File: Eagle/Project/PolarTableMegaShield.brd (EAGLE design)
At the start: 53.2 x 90.2 mm, 41 parts, among them IC2 LM358D, J10 LED + Radio, J3 Pi Connection, J5 IR Sensors, J6 Switch A + B, J7 Switch C + D, J8 Switch E + F, Q1 BC337, Q2 2N3906, Q3 2N3904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

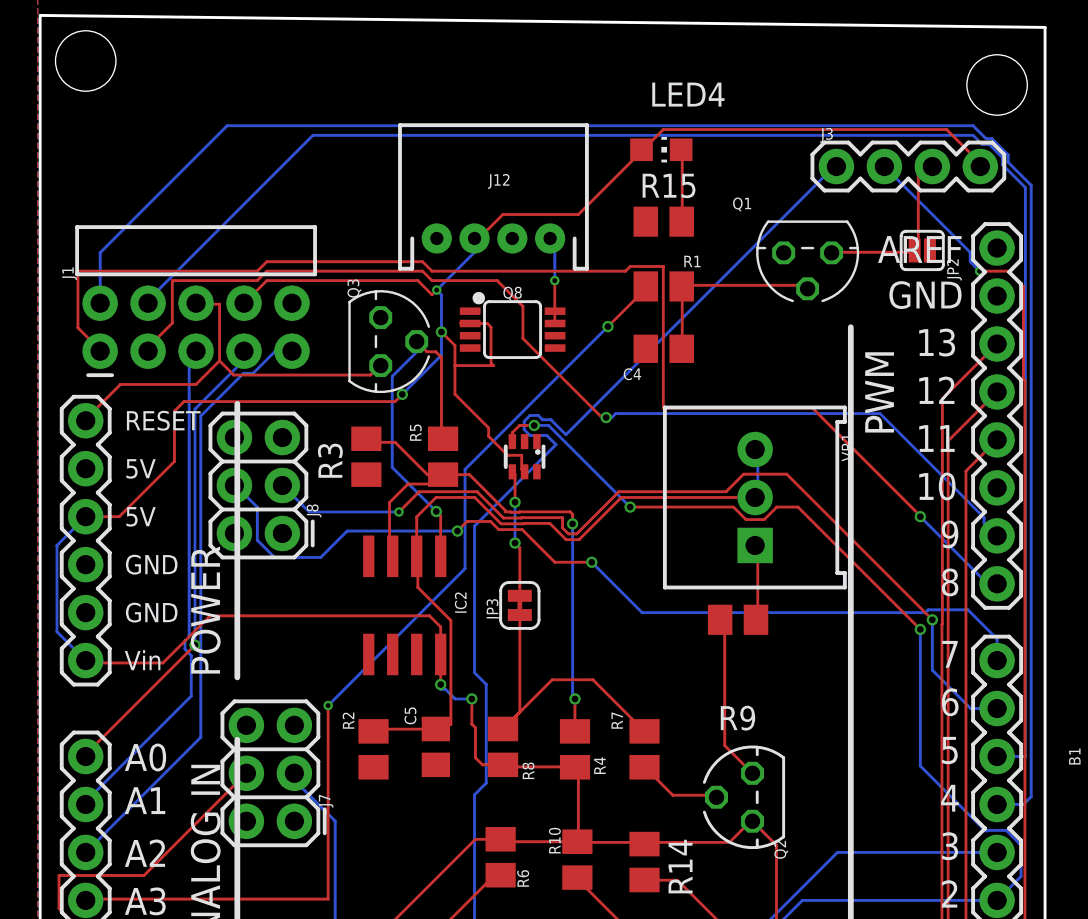
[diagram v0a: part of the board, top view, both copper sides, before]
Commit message: Changed the connector to be 6x2 so the shift reg could run at 3.3V
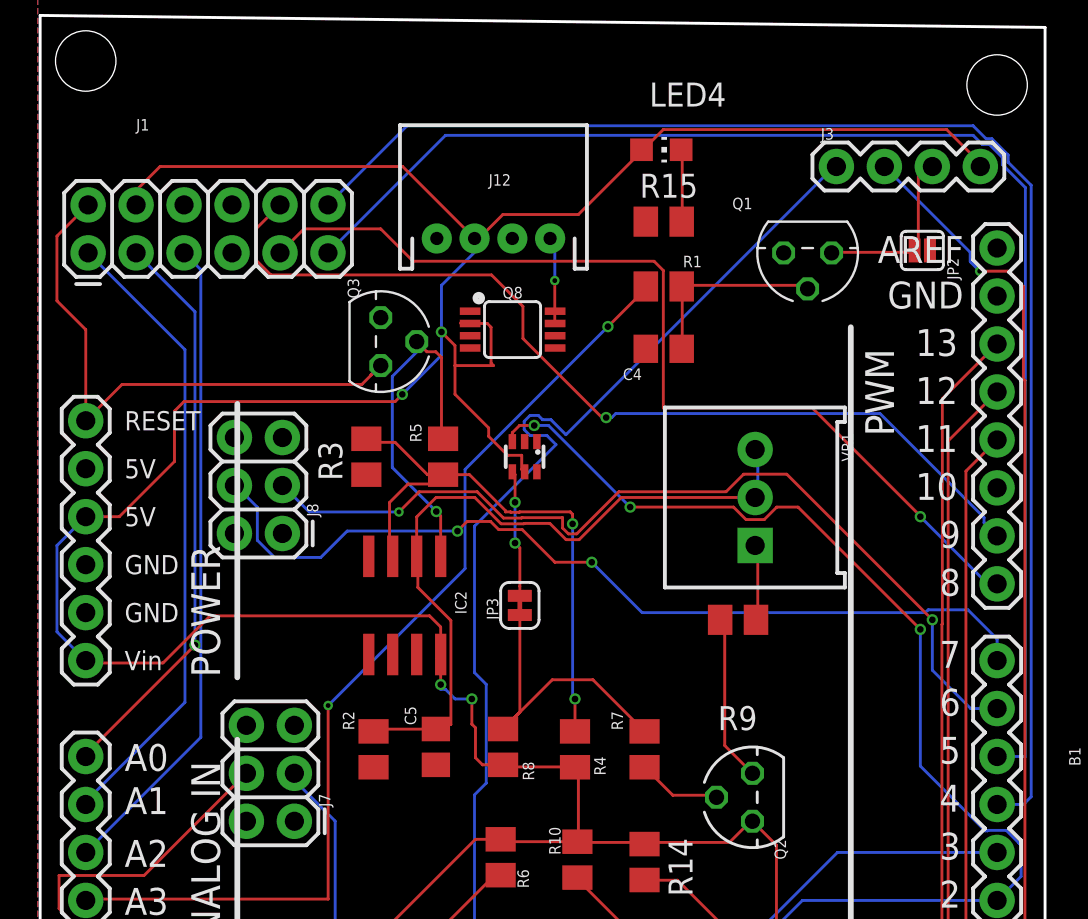
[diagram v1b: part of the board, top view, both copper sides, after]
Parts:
- J1: device SparkFun-Connectors:2X5-RA -> keir_library:2X6
- moved J1 6.94 mm to (2.54, 77.5), turned to 0 degrees
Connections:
- net !RES: now also J1.2; no longer J1.6
- net CLOCK: now also J1.1; no longer J1.5
- net DATA: now also J1.3; no longer J1.7
- net GND: now also J1.6, J1.8; no longer J1.10
- net LATCH: now also J1.5; no longer J1.9
- net VCC_1: now also J1.4; no longer J1.8
- net VCC_2: now also J1.7
- net XDIR: now also J1.10; no longer J1.3
- net XSTEP: now also J1.9; no longer J1.1
- net YDIR: now also J1.11; no longer J1.4
- net YSTEP: now also J1.12; no longer J1.2
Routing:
- net YSTEP: track 90.6 -> 74.9 mm
- net XSTEP: track 65.3 -> 50.6 mm
- net YDIR: track 83.2 -> 72.5 mm
- net VCC_1: track 222.1 -> 231.6 mm, vias 7 -> 6
- net !RES: track 21.7 -> 30.3 mm
- net CLOCK: track 26.7 -> 33.5 mm
- net DATA: track 24.9 -> 30.3 mm
- net XDIR: track 55.3 -> 50.1 mm
- net LATCH: track 31.9 -> 34.6 mm
